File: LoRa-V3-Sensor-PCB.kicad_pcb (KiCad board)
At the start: 2 copper layers, 10 x 10 mm, 6 parts, among them IC1 BME690, IC2 SHT40-BD1B-R2, IC3 TSL25911FN

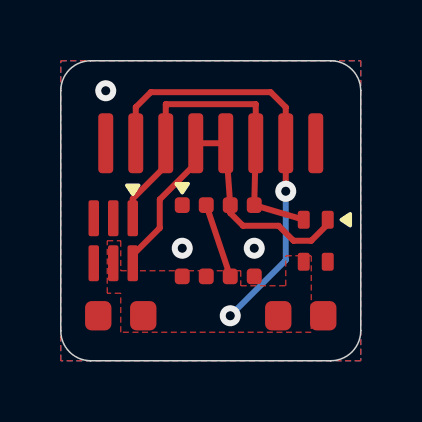
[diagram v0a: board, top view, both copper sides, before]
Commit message: fix missing 3d model for C0603
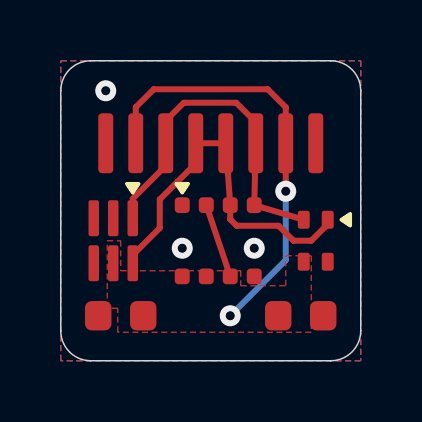
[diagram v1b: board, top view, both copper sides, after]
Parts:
- renumbered C2 to C1, C3 to C2
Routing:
- net SCL: track 12.3 -> 11.7 mm
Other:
- board text added: "${releaseDateShort}"
- board text added: "V${majorVersion}.${minorVersion}"
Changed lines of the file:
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@@
 		)
 	)
+	(property "majorVersion" "0")
+	(property "minorVersion" "2")
+	(property "releaseDate" "Wed Apr 16 13:20:30 2025")
+	(property "releaseDateShort" "2025-04-16")
 	(net 0 "")
 	(net 1 "GND")
@@
 		(fp_poly
 			(pts
-				(xy -1.85 -0.45) (xy -1.85 -0.85) (xy -1.55 -0.65)
+				(xy -1.9 -0.45) (xy -1.9 -0.85) (xy -1.6 -0.65)
 			)
 			(stroke
@@
 		(descr "Capacitor SMD 0603 (1608 Metric), square (rectangular) end terminal, IPC_7351 nominal, (Body size source: IPC-SM-782 page 76, https://www.pcb-3d.com/wordpress/wp-content/uploads/ipc-sm-782a_amendment_1_and_2.pdf), generated with kicad-footprint-generator")
 		(tags "capacitor")
-		(property "Reference" "C2"
+		(property "Reference" "C1"
 			(at 0 -1.43 0)
 			(layer "F.SilkS")
@@
 			(pintype "passive")
 		)
-		(model "C:/Users/pasca/Documents/Projects/Electronica/myComponents/1globallibraries/3dmodels/C0603_070.step"
+		(model "${KIPRJMOD}/inputs/3dmodels/C0603_070.step"
 			(offset
 				(xyz 0 0 0)
@@
 		(descr "Capacitor SMD 0603 (1608 Metric), square (rectangular) end terminal, IPC_7351 nominal, (Body size source: IPC-SM-782 page 76, https://www.pcb-3d.com/wordpress/wp-content/uploads/ipc-sm-782a_amendment_1_and_2.pdf), generated with kicad-footprint-generator")
 		(tags "capacitor")
-		(property "Reference" "C3"
+		(property "Reference" "C2"
 			(at 0 -1.43 0)
 			(layer "F.SilkS")
@@
 			(pintype "passive")
 		)
-		(model "C:/Users/pasca/Documents/Projects/Electronica/myComponents/1globallibraries/3dmodels/C0603_070.step"
+		(model "${KIPRJMOD}/inputs/3dmodels/C0603_070.step"
 			(offset
 				(xyz 0 0 0)
@@
 		(layer "User.1")
 	)
+	(gr_text "${releaseDateShort}"
+		(at 150.5 87.1 0)
+		(layer "B.SilkS")
+		(effects
+			(font
+				(size 0.8 0.8)
+				(thickness 0.1)
+			)
+			(justify bottom mirror)
+		)
+	)
+	(gr_text "V${majorVersion}.${minorVersion}"
+		(at 150.5 85.75 0)
+		(layer "B.SilkS")
+		(effects
+			(font
+				(size 1 1)
+				(thickness 0.1)
+			)
+			(justify bottom mirror)
+		)
+	)
 	(via
 		(at 149.55 89.55)
@@
 	)
 	(segment
+		(start 148.6 84.25)
+		(end 152.4 84.25)
+		(width 0.2)
+		(layer "F.Cu")
+		(net 4)
+	)
+	(segment
+		(start 152.4 84.25)
+		(end 153 84.85)
+		(width 0.2)
+		(layer "F.Cu")
+		(net 4)
+	)
+	(segment
+		(start 152.75 91.8)
+		(end 152.75 91.75)
+		(width 0.2)
+		(layer "F.Cu")
+		(net 4)
+	)
+	(segment
+		(start 148 86.05)
+		(end 148 84.85)
+		(width 0.2)
+		(layer "F.Cu")
+		(net 4)
+	)
+	(segment
 		(start 148 84.85)
-		(end 148.502253 84.347747)
+		(end 148.6 84.25)
+		(width 0.2)
+		(layer "F.Cu")
+		(net 4)
+	)
+	(segment
+		(start 150.35 88.1125)
+		(end 151.15 90.4875)
+		(width 0.2)
+		(layer "F.Cu")
+		(net 4)
+	)
+	(segment
+		(start 153 86.05)
+		(end 153 87.65)
 		(width 0.2)
 		(layer "F.Cu")
@@
 		(start 153 84.85)
 		(end 153 86.05)
-		(width 0.2)
-		(layer "F.Cu")
-		(net 4)
-	)
-	(segment
-		(start 148.502253 84.347747)
-		(end 152.497747 84.347747)
-		(width 0.2)
-		(layer "F.Cu")
-		(net 4)
-	)
-	(segment
-		(start 148 86.05)
-		(end 148 84.85)
-		(width 0.2)
-		(layer "F.Cu")
-		(net 4)
-	)
-	(segment
-		(start 152.75 91.8)
-		(end 152.75 91.75)
-		(width 0.2)
-		(layer "F.Cu")
-		(net 4)
-	)
-	(segment
-		(start 150.35 88.1125)
-		(end 151.15 90.4875)
-		(width 0.2)
-		(layer "F.Cu")
-		(net 4)
-	)
-	(segment
-		(start 153 86.05)
-		(end 153 87.65)
-		(width 0.2)
-		(layer "F.Cu")
-		(net 4)
-	)
-	(segment
-		(start 152.497747 84.347747)
-		(end 153 84.85)
 		(width 0.2)
 		(layer "F.Cu")
@@
 	)
 	(segment
-		(start 152 84.747747)
-		(end 152 86.05)
-		(width 0.2)
-		(layer "F.Cu")
-		(net 5)
-	)
-	(segment
 		(start 152 86.05)
 		(end 151.95 88.1125)
@@
 	)
 	(segment
-		(start 149 84.747747)
-		(end 152 84.747747)
+		(start 149 86.05)
+		(end 149 85.3)
+		(width 0.2)
+		(layer "F.Cu")
+		(net 5)
+	)
+	(segment
+		(start 152 85.35)
+		(end 152 86.05)
+		(width 0.2)
+		(layer "F.Cu")
+		(net 5)
+	)
+	(segment
+		(start 149.6 84.7)
+		(end 151.35 84.7)
 		(width 0.2)
 		(layer "F.Cu")
@@
 	)
 	(segment
-		(start 149 86.05)
-		(end 149 84.747747)
+		(start 151.35 84.7)
+		(end 152 85.35)
+		(width 0.2)
+		(layer "F.Cu")
+		(net 5)
+	)
+	(segment
+		(start 149 85.3)
+		(end 149.6 84.7)
 		(width 0.2)
 		(layer "F.Cu")
@@
 	)
 	(segment
+		(start 153.260191 89.3)
+		(end 153.85 89.3)
+		(width 0.2)
+		(layer "F.Cu")
+		(net 6)
+	)
+	(segment
+		(start 153.85 89.3)
+		(end 154.4 88.75)
+		(width 0.2)
+		(layer "F.Cu")
+		(net 6)
+	)
+	(segment
+		(start 151.15 88.1125)
+		(end 151.15 88.587499)
+		(width 0.2)
+		(layer "F.Cu")
+		(net 6)
+	)
+	(segment
+		(start 150 86.05)
+		(end 151 86.05)
+		(width 0.2)
+		(layer "F.Cu")
+		(net 6)
+	)
+	(segment
+		(start 148.8 88.875)
+		(end 148.8 87.923873)
+		(width 0.2)
+		(layer "F.Cu")
+		(net 6)
+	)
+	(segment
 		(start 154.4 88.75)
 		(end 154.4 88.6)
@@
 	)
 	(segment
-		(start 151.15 88.1125)
-		(end 151.15 88.374999)
-		(width 0.2)
-		(layer "F.Cu")
-		(net 6)
-	)
-	(segment
-		(start 150 86.05)
-		(end 151 86.05)
-		(width 0.2)
-		(layer "F.Cu")
-		(net 6)
-	)
-	(segment
-		(start 148.8 88.875)
-		(end 148.8 87.923873)
-		(width 0.2)
-		(layer "F.Cu")
-		(net 6)
-	)
-	(segment
-		(start 153.85 89.3)
-		(end 154.4 88.75)
-		(width 0.2)
-		(layer "F.Cu")
-		(net 6)
-	)
-	(segment
-		(start 151.15 88.374999)
-		(end 151.575001 88.8)
-		(width 0.2)
-		(layer "F.Cu")
-		(net 6)
-	)
-	(segment
 		(start 147.9 89.775)
 		(end 148.8 88.875)
@@
 	)
 	(segment
+		(start 151.15 88.587499)
+		(end 151.362501 88.8)
+		(width 0.2)
+		(layer "F.Cu")
+		(net 6)
+	)
+	(segment
 		(start 148.8 87.923873)
 		(end 150 86.723873)
@@
 	)
 	(segment
-		(start 153.260191 89.3)
-		(end 153.85 89.3)
-		(width 0.2)
-		(layer "F.Cu")
-		(net 6)
-	)
-	(segment
-		(start 151.575001 88.8)
+		(start 151.362501 88.8)
 		(end 152.760191 88.8)
 		(width 0.2)
@@
 		(polygon
 			(pts
-				(xy 147.5 92.35) (xy 147.5 91.05) (xy 147.05 91.05) (xy 147.05 89.3) (xy 147.5 89.3) (xy 147.5 90.3)
+				(xy 147.4 92.35) (xy 147.4 91.55) (xy 147.05 91.55) (xy 147.05 89.3) (xy 147.5 89.3) (xy 147.5 90.3)
 				(xy 151.5 90.3) (xy 151.5 90.8) (xy 153 90.8) (xy 153 89.8) (xy 153.85 89.8) (xy 153.85 92.35)
 			)
